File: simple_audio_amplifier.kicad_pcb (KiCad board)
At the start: 2 copper layers, 28 parts, among them J1 Screw_Terminal_01x02, J2 PJ-322, J3 Screw_Terminal_01x02, Q1 2N2222A, U1 LM386N-1

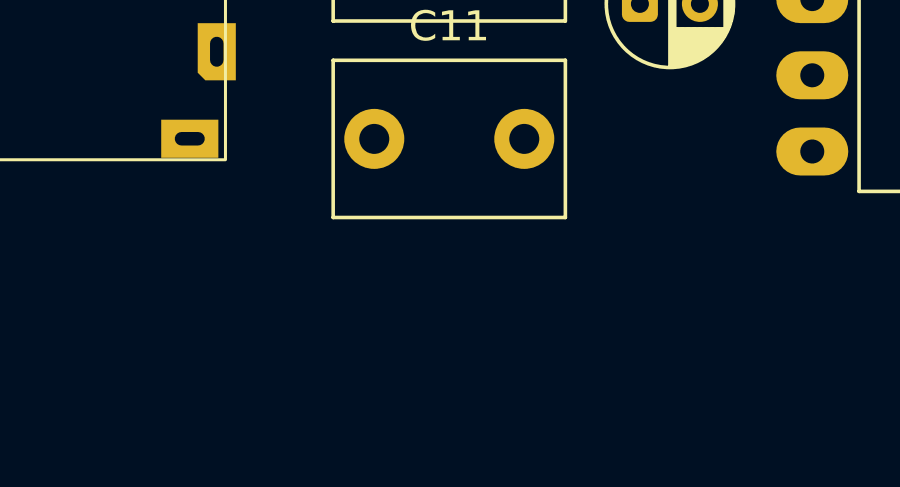
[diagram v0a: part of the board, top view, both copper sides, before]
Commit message: Added component
Feat: added further capacitor on the input power line.
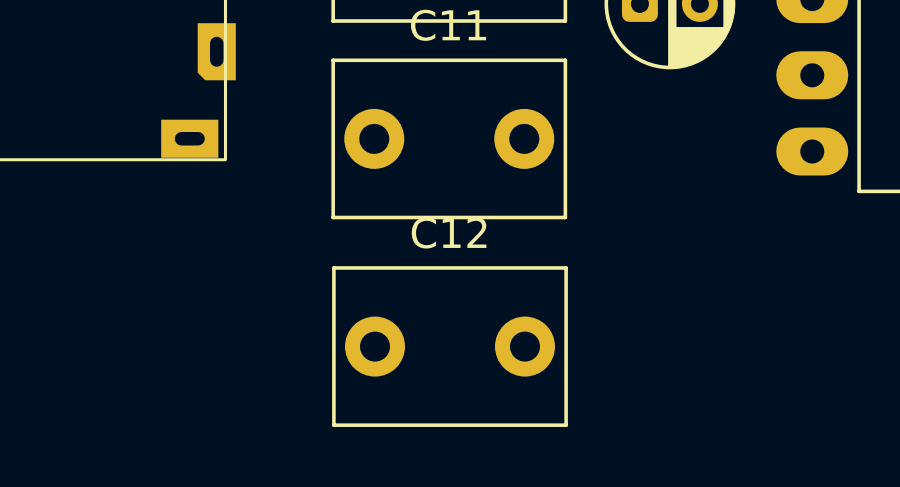
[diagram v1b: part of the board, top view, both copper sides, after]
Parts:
- added C12: 0.1 uF, Capacitor_THT:C_Disc_D7.5mm_W5.0mm_P5.00mm, F.Cu at (143.6, 123.8)
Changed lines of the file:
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@@
+		)
+	)
+	(footprint "Capacitor_THT:C_Disc_D7.5mm_W5.0mm_P5.00mm"
+		(layer "F.Cu")
+		(at 143.6408 123.7996)
+		(descr "C, Disc series, Radial, pin pitch=5.00mm, diameter*width=7.5*5.0mm^2, Capacitor, http://www.vishay.com/docs/28535/vy2series.pdf")
+		(tags "C Disc series Radial pin pitch 5.00mm diameter 7.5mm width 5.0mm Capacitor")
+		(property "Reference" "C12"
+			(at 2.5 -3.75 0)
+			(layer "F.SilkS")
+			(effects
+				(font
+					(size 1 1)
+					(thickness 0.15)
+				)
+			)
+		)
+		(property "Value" "0.1 uF"
+			(at 2.5 3.75 0)
+			(layer "F.Fab")
+			(effects
+				(font
+					(size 1 1)
+					(thickness 0.15)
+				)
+			)
+		)
+		(property "Datasheet" "~"
+			(at 0 0 0)
+			(layer "F.Fab")
+			(hide yes)
+			(effects
+				(font
+					(size 1.27 1.27)
+					(thickness 0.15)
+				)
+			)
+		)
+		(property "Description" "Unpolarized capacitor"
+			(at 0 0 0)
+			(layer "F.Fab")
+			(hide yes)
+			(effects
+				(font
+					(size 1.27 1.27)
+					(thickness 0.15)
+				)
+			)
+		)
+		(property ki_fp_filters "C_*")
+		(sheetname "/")
+		(sheetfile "simple_audio_amplifier.kicad_sch")
+		(attr through_hole)
+		(fp_line
+			(start -1.37 -2.62)
+			(end 6.37 -2.62)
+			(stroke
+				(width 0.12)
+				(type solid)
+			)
+			(layer "F.SilkS")
+		)
+		(fp_line
+			(start -1.37 2.62)
+			(end -1.37 -2.62)
+			(stroke
+				(width 0.12)
+				(type solid)
+			)
+			(layer "F.SilkS")
+		)
+		(fp_line
+			(start 6.37 -2.62)
+			(end 6.37 2.62)
+			(stroke
+				(width 0.12)
+				(type solid)
+			)
+			(layer "F.SilkS")
+		)
+		(fp_line
+			(start 6.37 2.62)
+			(end -1.37 2.62)
+			(stroke
+				(width 0.12)
+				(type solid)
+			)
+			(layer "F.SilkS")
+		)
+		(fp_rect
+			(start -1.5 -2.75)
+			(end 6.5 2.75)
+			(stroke
+				(width 0.05)
+				(type solid)
+			)
+			(fill no)
+			(layer "F.CrtYd")
+		)
+		(fp_rect
+			(start -1.25 -2.5)
+			(end 6.25 2.5)
+			(stroke
+				(width 0.1)
+				(type solid)
+			)
+			(fill no)
+			(layer "F.Fab")
+		)
+		(fp_text user "${REFERENCE}"
+			(at 2.5 0 0)
+			(layer "F.Fab")
+			(effects
+				(font
+					(size 1 1)
+					(thickness 0.15)
+				)
+			)
+		)
+		(pad "1" thru_hole circle
+			(at 0 0)
+			(size 2 2)
+			(drill 1)
+			(layers "*.Cu" "*.Mask")
+			(remove_unused_layers no)
+			(net 3 "GND")
+			(pintype "passive")
+		)
+		(pad "2" thru_hole circle
+			(at 5 0)
+			(size 2 2)
+			(drill 1)
+			(layers "*.Cu" "*.Mask")
+			(remove_unused_layers no)
+			(net 4 "+BATT")
+			(pintype "passive")
+		)
+		(embedded_fonts no)
+		(model "${KICAD9_3DMODEL_DIR}/Capacitor_THT.3dshapes/C_Disc_D7.5mm_W5.0mm_P5.00mm.step"
+			(offset
+				(xyz 0 0 0)
+			)
+			(scale
+				(xyz 1 1 1)
+			)
+			(rotate
+				(xyz 0 0 0)
+			)
 		)
 	)

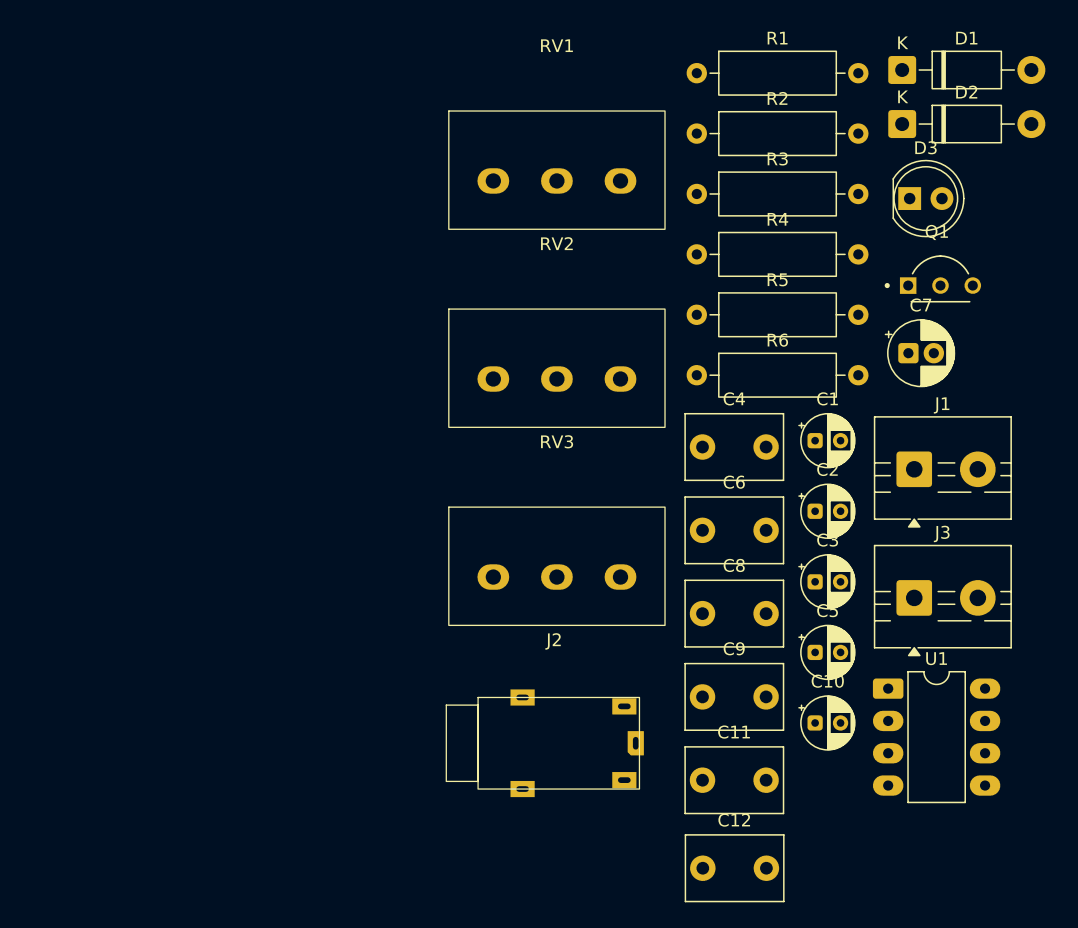
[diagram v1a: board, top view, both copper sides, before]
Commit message: Component arrangement on the PCB
Feat: identified a first positioning of the components on the PCB layout. Work in progress.
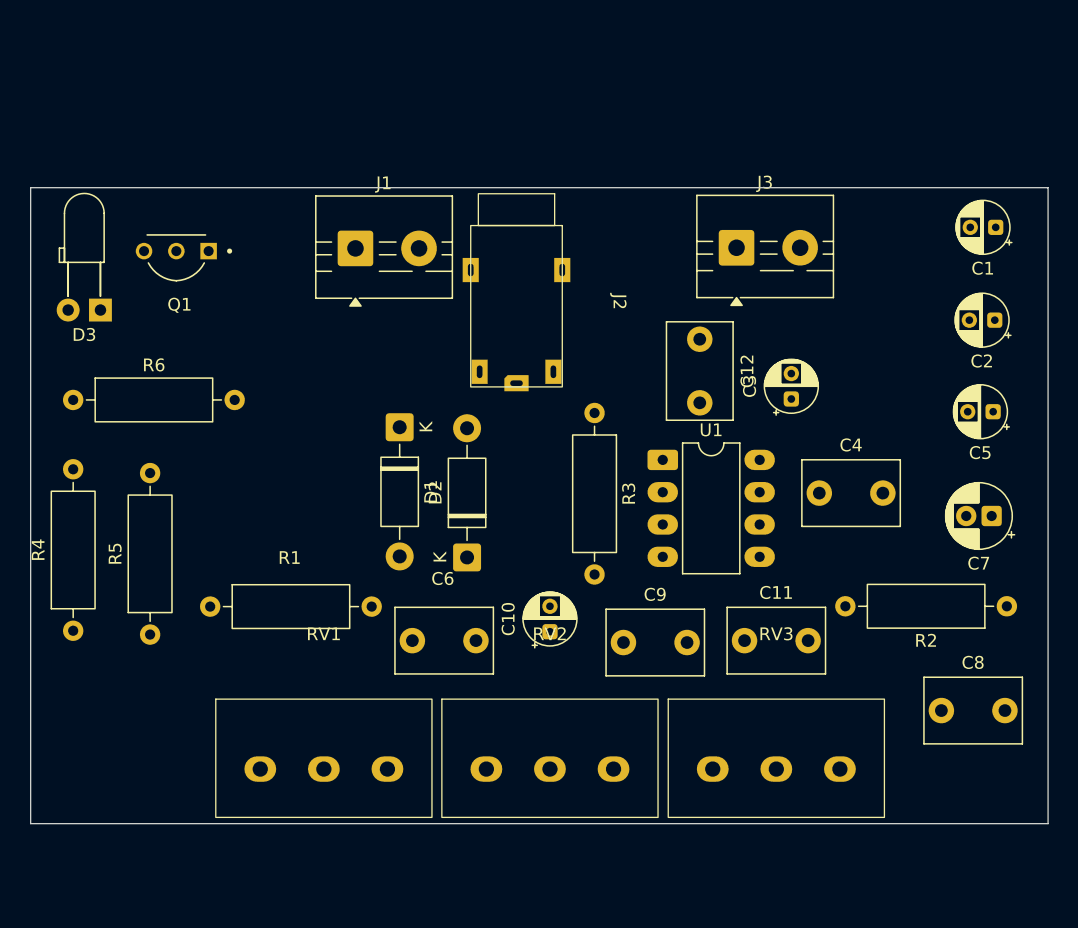
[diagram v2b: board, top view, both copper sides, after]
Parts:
- D3: footprint LED_THT:LED_D5.0mm -> LED_THT:LED_D3.0mm_Horizontal_O3.81mm_Z2.0mm
- moved D3 64.2 mm to (96.3, 79.9), turned to 180 degrees
- moved Q1 60.1 mm to (102.2, 77.6), turned to 180 degrees
- moved R4 57.3 mm to (94.1, 105.1), turned to 90 degrees
- moved R1 56.8 mm to (104.9, 103.2)
- moved R5 49.8 mm to (100.2, 105.4), turned to 90 degrees
- moved RV1 49.7 mm to (113.8, 105.9)
- moved R6 49.1 mm to (94.1, 87.0)
- moved D1 48.5 mm to (119.8, 89.1), turned to -90 degrees
- moved D2 48.3 mm to (125.1, 99.4), turned to 90 degrees
- moved J1 47.3 mm to (116.3, 75.1)
- moved R2 44.5 mm to (167.6, 103.2), turned to 180 degrees
- moved C12 41.6 mm to (143.4, 82.2), turned to -90 degrees
- moved J3 30.9 mm to (146.3, 75.0)
- moved RV2 30.7 mm to (131.6, 105.9)
- moved J2 27.5 mm to (136.6, 79.3), turned to -90 degrees
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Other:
- board outline added: 80 x 50 mm

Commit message: New components + 3D assignments
Feat: added input switch S1.
Feat: added protection zenere D4.
Feat: defined the terminal blocks J1, J3 with part number.
Feat: added the 3D models where available.
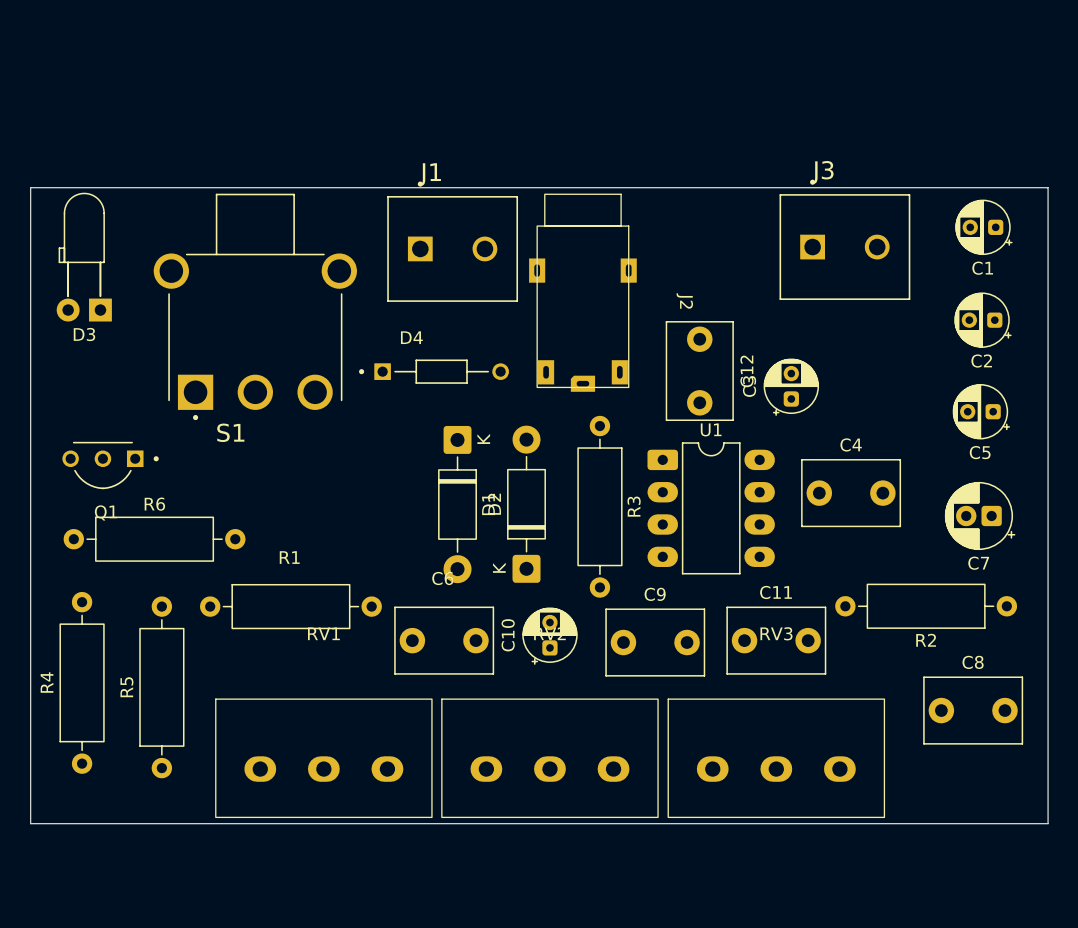
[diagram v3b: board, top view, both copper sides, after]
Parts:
- added D4: NZX13B,133, NZX13B,133:DIOAD928W47L399D179, F.Cu at (123.1, 84.8)
- added S1: 500SSP3S1M6QEA, 500SSP3S1M6QEA:SW_500SSP3S1M6QEA, F.Cu at (108.5, 81.6)
- J1, J3: value Screw_Terminal_01x02 -> TB006-508-02BE; footprint TerminalBlock:TerminalBlock_MaiXu_MX126-5.0-02P_1x02_P5.00mm -> TB006 -508-02BE:CUI_TB006_-508-02BE
- moved Q1 17.3 mm to (96.5, 93.9)
- moved R6 11.0 mm to (94.2, 97.9)
- moved R5 10.5 mm to (101.1, 115.9)
- moved R4 10.5 mm to (94.8, 115.6)
- moved J3 5.98 mm to (152.3, 75.0)
- moved J2 5.22 mm to (141.8, 79.3)
- moved J1 5.10 mm to (121.4, 75.1)
- moved D2 4.76 mm to (129.8, 100.3)
- moved D1 4.66 mm to (124.3, 90.1)
- moved C10 1.27 mm to (131.6, 106.5)
- moved R3 1.11 mm to (135.6, 89.0)
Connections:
- J1 pad 1: +BATT -> Net-(J1-Pin_1)

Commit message: Put down traces on PCB layout
Feat: connected all the nets in the PCB (no errors).
Feat: added mounting hole components both on schematics and PCB.
Docs: added the links for the components that will be used.
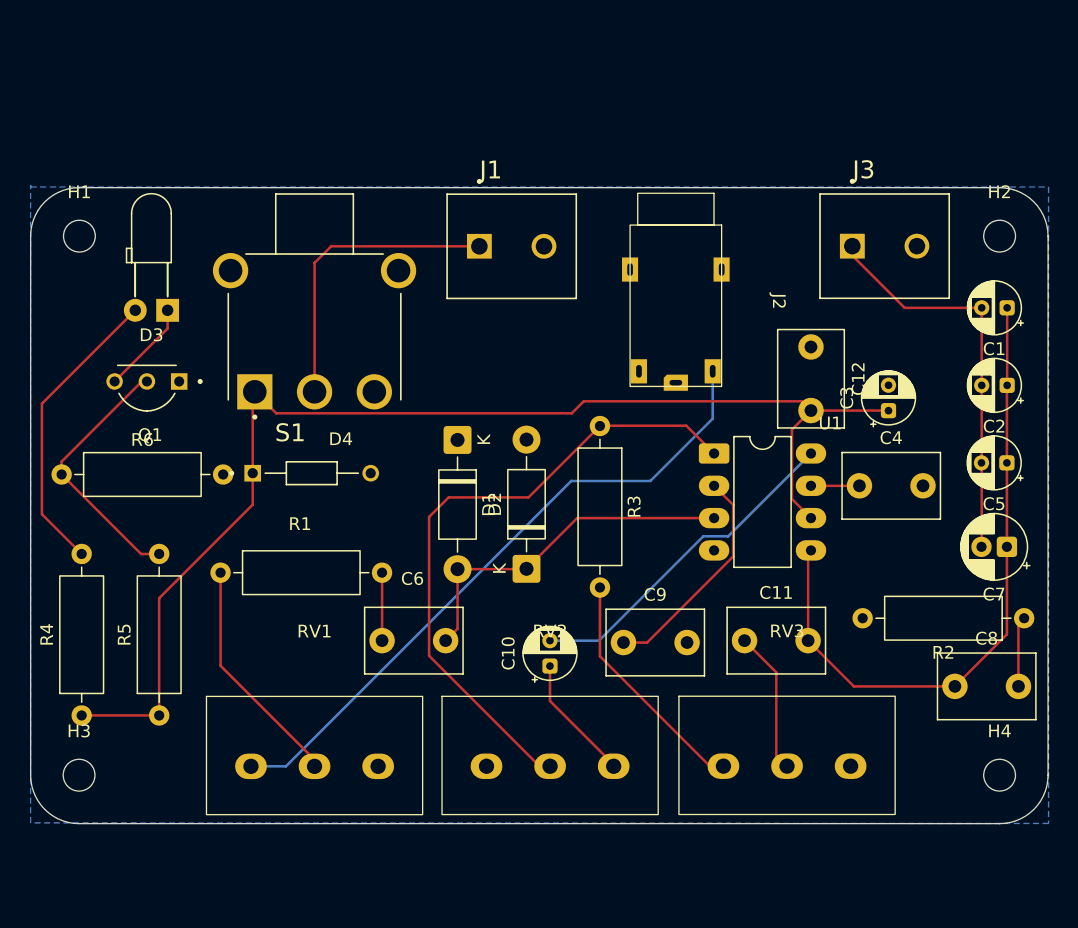
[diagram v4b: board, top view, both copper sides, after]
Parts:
- added H1: MountingHole, MountingHole:MountingHole_2.5mm, F.Cu at (94.6, 74.1)
- added H2: MountingHole, MountingHole:MountingHole_2.5mm, F.Cu at (167.0, 74.1)
- added H3: MountingHole, MountingHole:MountingHole_2.5mm, F.Cu at (94.6, 116.5)
- added H4: MountingHole, MountingHole:MountingHole_2.5mm, F.Cu at (167.0, 116.5)
- C8: value 0.068 uF -> 68 nF
- moved D4 13.0 mm to (112.9, 92.7)
- moved C12 8.77 mm to (152.1, 82.8)
- moved C3 7.70 mm to (158.2, 87.8)
- moved J2 7.31 mm to (149.1, 79.2)
- moved Q1 6.99 mm to (99.9, 87.9)
- moved C1 6.39 mm to (167.6, 79.7)
- moved D3 5.28 mm to (101.5, 79.9)
- moved C2 5.22 mm to (167.6, 85.8)
- moved R6 5.18 mm to (93.2, 92.8)
- moved S1 4.66 mm to (113.1, 81.6)
- moved J1 4.65 mm to (126.1, 74.9)
- moved C5 4.17 mm to (167.6, 91.9)
- moved R5 4.14 mm to (100.9, 111.8)
- moved U1 4.07 mm to (144.5, 91.2)
- moved R4 3.79 mm to (94.8, 111.8)
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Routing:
- net +BATT: track 0.00 -> 95.6 mm
- net Net-(C1-Pad1): track 0.00 -> 51.7 mm
- net Net-(J2-Pad2): track 0.00 -> 51.4 mm
- net Net-(R3-Pad1): track 0.00 -> 50.4 mm
- net Net-(J3-Pin_1): track 0.00 -> 31.4 mm
- net Net-(D1-A): track 0.00 -> 27.8 mm
- net Net-(C10-Pad2): track 0.00 -> 26.6 mm
- net Net-(J1-Pin_1): track 0.00 -> 23.6 mm
- net Net-(D3-A): track 0.00 -> 23.5 mm
- net Net-(Q1-Pad2): track 0.00 -> 20.6 mm
- net Net-(R1-Pad1): track 0.00 -> 18.8 mm
- net Net-(R3-Pad2): track 0.00 -> 18.0 mm
- net Net-(U1--): track 0.00 -> 17.6 mm
- net Net-(C11-Pad1): track 0.00 -> 11.1 mm
- net Net-(C10-Pad1): track 0.00 -> 10.00 mm
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- added copper zone on B.Cu, net GND
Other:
- outline, holes or cut-outs redrawn

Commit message: Completition of the PCB + BOM
Fix: changed the type of the rotary potentiometer to THT.
Fix: changed the type of the input jack to THT and fixed the silkscreen.
Feat: moved the general silkscreen to avoid any error/warning.
Docs: released the BOM with a part number for every single component.
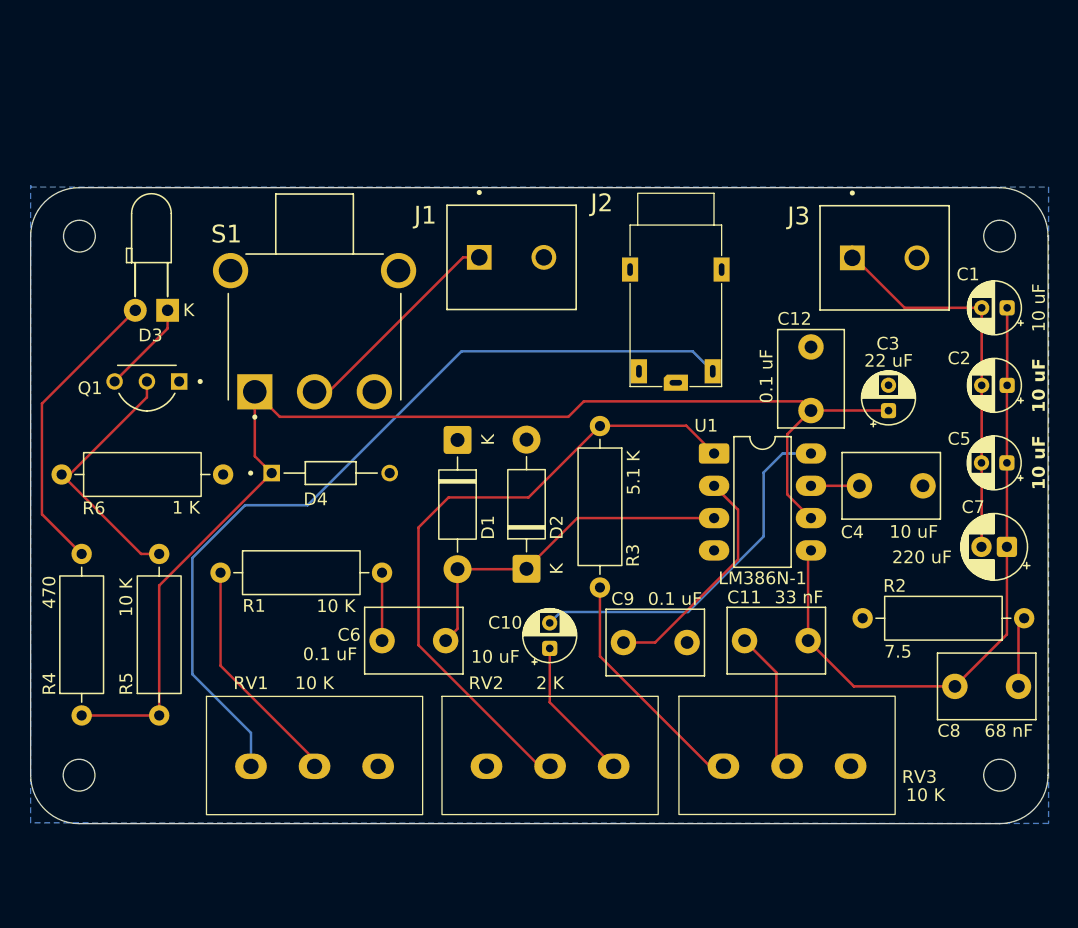
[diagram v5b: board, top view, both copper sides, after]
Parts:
- added REF**: OSHW-Logo_5.7x6mm_SilkScreen, Symbol:OSHW-Logo_5.7x6mm_SilkScreen, B.Cu at (128.9, 81.7)
- added REF**: KiCad-Logo_5mm_SilkScreen, Symbol:KiCad-Logo_5mm_SilkScreen, B.Cu at (113.1, 82.1)
- moved D4 1.49 mm to (114.4, 92.7)
- moved C10 1.39 mm to (131.6, 106.5)
- moved J3 0.92 mm to (155.4, 75.8)
- moved J1 0.87 mm to (126.1, 75.8)
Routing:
- net Net-(J2-Pad2): track 51.4 -> 66.6 mm
- net Net-(J1-Pin_1): track 23.6 -> 17.3 mm
- net Net-(C10-Pad2): track 26.6 -> 29.0 mm
- net +BATT: track 95.6 -> 97.2 mm
- net Net-(C10-Pad1): track 10.00 -> 11.4 mm
- net Net-(R3-Pad1): track 50.4 -> 51.1 mm
- net Net-(U1--): track 17.6 -> 18.3 mm
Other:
- board text added: "Bass Boost"
- board text added: "Designed by: F.G."
- board text added: "Gain"
- board text added: "Input (4-12V)"
- board text added: "Input Jack"
- board text added: "K"
- board text added: "ON-OFF Switch"
- board text added: "Output (SPEAKER)"
- board text added: "SIMPLE AUDIO AMPLIFIER"
- board text added: "Version: 1.0"
- board text added: "Volume"

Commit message: Moved labels on schematics + more info on PCB
Fix: moved the various label on the schematics to make it more readable.
Docs: added board characteristics on PCB.
Docs: added vertical and horizontal sizes on PCB.
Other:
- board text added: "0,1000 mm / 0,1000 mm"
- board text added: "0,3000 mm"
- board text added: "1,6000 mm"
- board text added: "2"
- board text added: "80,0100 mm x 50,0109 mm"
- board text added: "BOARD CHARACTERISTICS"
- board text added: "Board Thickness:"
- board text added: "Board overall dimensions:"
- board text added: "Castellated pads:"
- board text added: "Copper Finish:"
- board text added: "Copper Layer Count:"
- board text added: "Edge card connectors:"
- board text added: "Impedance Control:"
- board text added: "Min hole diameter:"
- board text added: "Min track/spacing:"
- board text added: "No"
- board text added: "None"
- board text added: "Plated Board Edge:"
